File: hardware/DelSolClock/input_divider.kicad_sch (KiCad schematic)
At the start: 3 parts

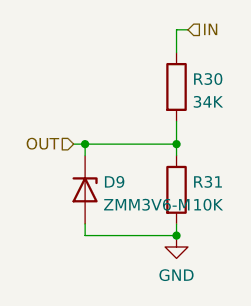
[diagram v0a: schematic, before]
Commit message: added missing 3V3 connection to the accelerometer CS pin, to select I2C mode.
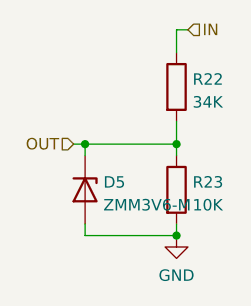
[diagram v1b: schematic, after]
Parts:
- renumbered D9 to D5, R30 to R22, R31 to R23
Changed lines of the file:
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@@
 		(dnp no)
 		(fields_autoplaced yes)
-		(property "Reference" "#PWR046"
+		(property "Reference" "#PWR042"
 			(at 142.24 114.3 0)
 			(effects
@@
 		(dnp no)
 		(fields_autoplaced yes)
-		(property "Reference" "R31"
+		(property "Reference" "R23"
 			(at 144.018 102.0353 0)
 			(effects
@@
 		(dnp no)
 		(fields_autoplaced yes)
-		(property "Reference" "R30"
+		(property "Reference" "R22"
 			(at 144.018 90.6053 0)
 			(effects
@@
 		(dnp no)
 		(fields_autoplaced yes)
-		(property "Reference" "D9"
+		(property "Reference" "D5"
 			(at 134.112 102.0353 90)
 			(effects
